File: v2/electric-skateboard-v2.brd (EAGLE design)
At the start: 88.9 x 55.9 mm, 60 parts, among them J1 ZX62D-B-5P8, U1 SPX29300, U2 LDO, U3 MPU-9150, U5 STM32F4V

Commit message: In theory I could ship this layout but I'm ashamed of it. It's gross.
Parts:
- removed TP3, TP4: TPTP06R, testpad:TP06R
- CTS1: value 25MHz -> (none); device crystal:CTS406 -> adafruit:CTS406
- JP6: value (none) -> PRESSA
- JP7: value (none) -> PRESSB
- JP9: value (none) -> LCD
- moved JP9 153.5 mm to (28.7, 51.6), turned to 180 degrees
- moved JP8 130.1 mm to (54.9, 21.8), turned to 180 degrees
- moved C9 122.6 mm to (40.4, 22.9), turned to 90 degrees
- moved R17 121.8 mm to (47.2, 22.1), turned to 270 degrees
- moved R15 116.3 mm to (47.2, 19.1), turned to 90 degrees
- moved JTAG1 104.4 mm to (36.1, 21.1), turned to 0 degrees
- moved JP7 100.6 mm to (11.7, 23.6)
- moved R14 91.3 mm to (22.6, 21.8), turned to 270 degrees
- moved JP6 89.9 mm to (11.7, 18.5)
- moved JP4 88.1 mm to (34.3, 53.1)
- moved C15 87.4 mm to (33.5, 44.7), turned to 0 degrees
- moved J1 87.4 mm to (2.03, 5.08), turned to 270 degrees
- moved C18 86.1 mm to (33.5, 45.8), turned to 0 degrees
- moved Q2 82.9 mm to (46.5, 48.3)
- moved R12 81.4 mm to (7.62, 18.5), turned to 90 degrees
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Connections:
- net N$1 renamed SDA2
- net N$10 renamed ESCB
- net N$12 renamed ESCA
- net N$7 renamed SCL2
- net CLKOUT: now also U5.PE1; no longer U5.PD9
- net GND: no longer TP3.TP, TP4.TP
- net INT: now also U5.PE0; no longer U5.PD8
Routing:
- net 5V: track 2.61 -> 109.5 mm, vias 0 -> 2
- net ANALOG_IN_PC3: track 0.00 -> 67.7 mm, vias 0 -> 2
- net HALLA_DIGINPUT: track 0.00 -> 59.8 mm, vias 0 -> 2
- net FS_VBUS: track 0.00 -> 58.8 mm, vias 0 -> 2
- net FS_ID: track 0.00 -> 58.5 mm, vias 0 -> 2
- net 3.3V: track 13.8 -> 72.1 mm, vias 0 -> 11
- net FS_DP: track 0.00 -> 56.6 mm, vias 0 -> 2
- net HALLB_DIGINPUT: track 0.00 -> 55.3 mm, vias 0 -> 2
- net FS_DM: track 0.00 -> 54.3 mm, vias 0 -> 2
- net ANALOG_IN_PC2: track 0.00 -> 50.8 mm, vias 0 -> 2
- net SCL1: track 0.00 -> 33.8 mm
- net CLKOUT: track 0.00 -> 33.7 mm, vias 0 -> 2
- net VIN: track 0.00 -> 30.7 mm
- net INT: track 0.00 -> 27.9 mm, vias 0 -> 2
- net SDA1: track 0.00 -> 27.2 mm, vias 0 -> 2
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- added copper zone on layer 1, net 3.3V
- added copper zone on layer 16, net 5V
- added copper zone on layer 1, net GND
- added copper zone on layer 16, net GND
- added copper zone on layer 1, net OSC_IN1
- added copper zone on layer 1, net OSC_OUT1
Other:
- board size 88.9 x 55.9 mm -> 59.4 x 55.9 mm

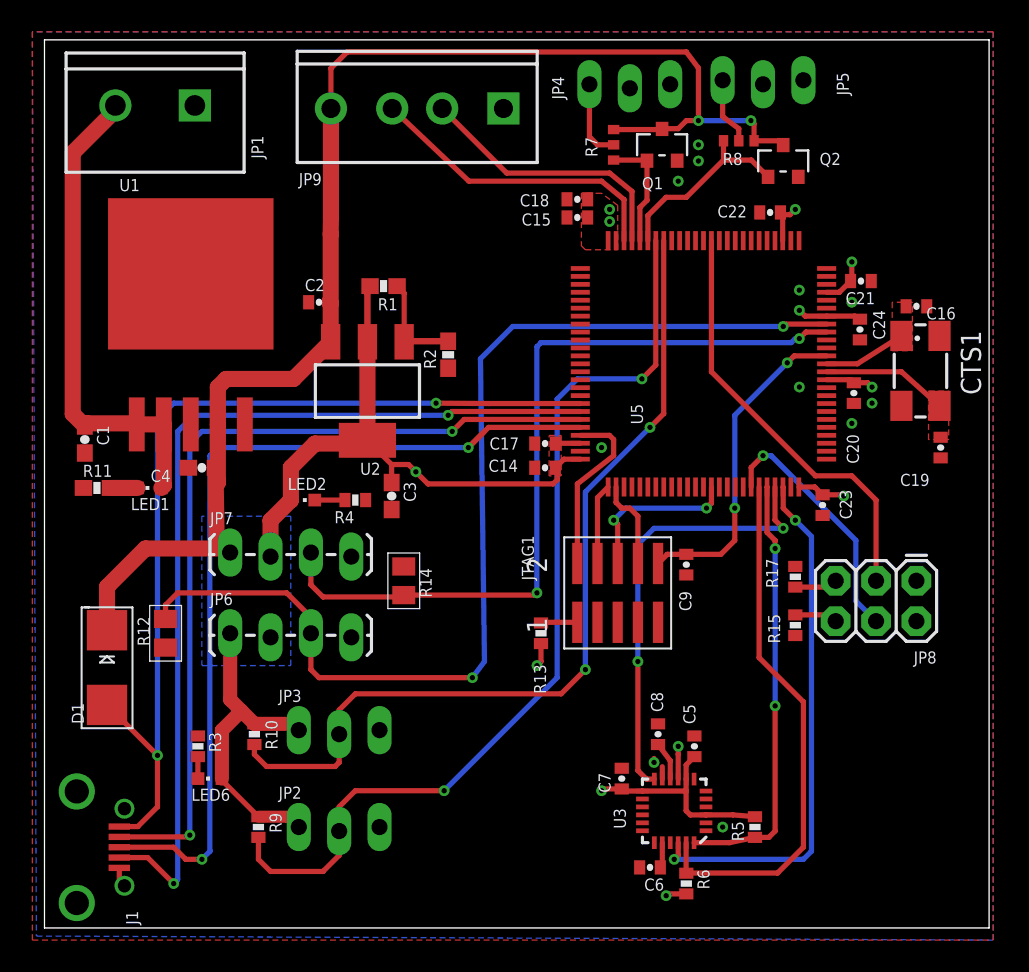
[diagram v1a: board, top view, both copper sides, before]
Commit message: Needs final review but otherwise layout is done.
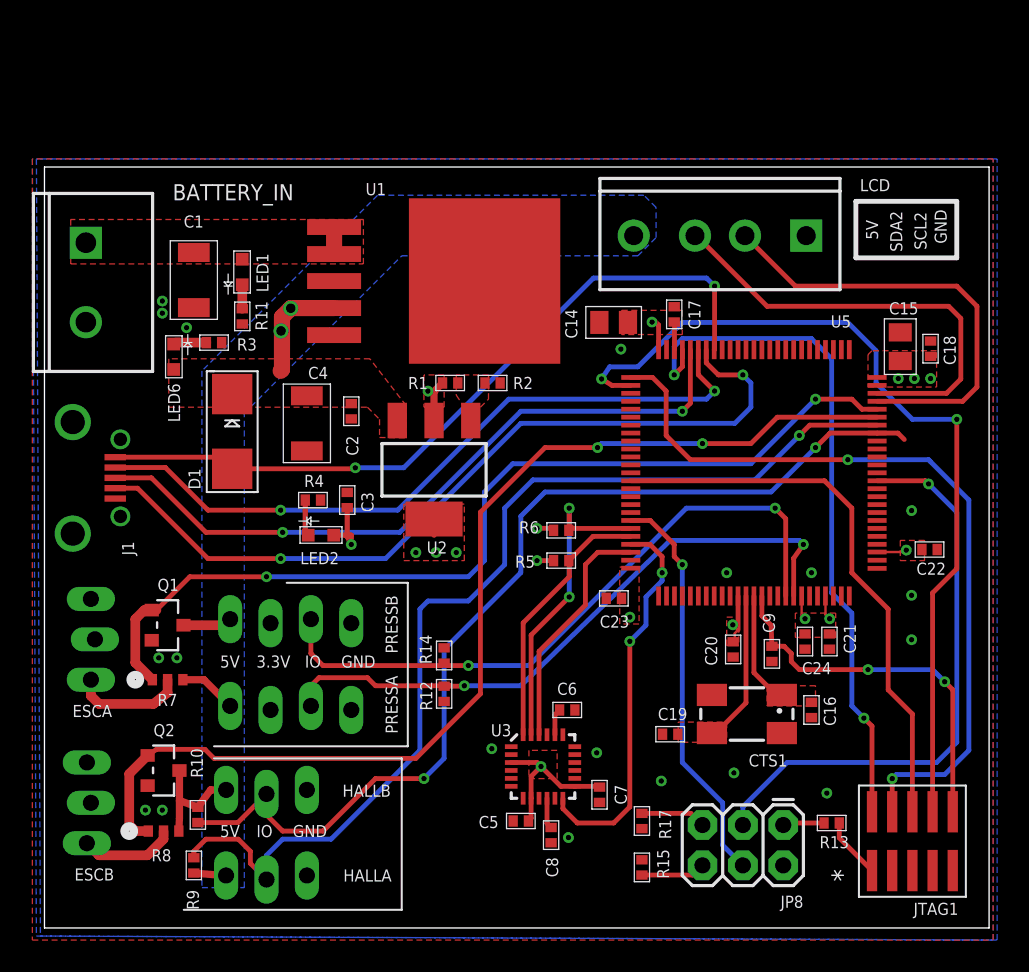
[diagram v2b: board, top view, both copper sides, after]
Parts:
- removed JP1: BATT, SparkFun-Connectors:SCREWTERMINAL-5MM-2
- removed JP2: HALLA, SparkFun-Connectors:1X03_LOCK_LONGPADS
- removed JP3: HALLB, SparkFun-Connectors:1X03_LOCK_LONGPADS
- removed JP4: ESCA, SparkFun-Connectors:1X03_LOCK_LONGPADS
- removed JP5: ESCB, SparkFun-Connectors:1X03_LOCK_LONGPADS
- removed JP6: PRESSA, SparkFun-Connectors:1X04_LOCK_LONGPADS
- removed JP7: PRESSB, SparkFun-Connectors:1X04_LOCK_LONGPADS
- removed JP9: LCD, SparkFun-Connectors:SCREWTERMINAL-3.5MM-4_LOCK
- added BATTERY_IN: BATT, SparkFun-Connectors:SCREWTERMINAL-5MM-2
- added ESCA, ESCB, HALLA, HALLB: (no value), SparkFun-Connectors:1X03_LOCK_LONGPADS
- added LCD: (no value), SparkFun-Connectors:SCREWTERMINAL-3.5MM-4_LOCK
- added PRESSA, PRESSB: (no value), SparkFun-Connectors:1X04_LOCK_LONGPADS
- C1, C4: device SparkFun-Passives:0603-CAP -> max-viz:RLC-1210
- C14, C15: device SparkFun-Passives:0402-CAP -> max-viz:RLC-0805
- C16, C17, C18, C19, C2, C20, C21, C22, C23, C24, C5, C6, C7, C8, C9: device SparkFun-Passives:0402-CAP -> max-viz:RLC-0402
- C3: device SparkFun-Passives:0603-CAP -> max-viz:RLC-0402
- LED1, LED2, LED6: device led:CHIPLED_0603 -> max-viz:LED0603
- R1, R11, R2: device SparkFun-Passives:0603-RES -> max-viz:RLC-0402
- R10, R13, R15, R17, R3, R4, R5, R6, R9: device SparkFun-Passives:0402-RES -> max-viz:RLC-0402
- R12, R14: device max-viz:RLC-0805 -> max-viz:RLC-0402
- moved R8 56.5 mm to (7.49, 6.10)
- moved Q2 54.7 mm to (7.49, 9.91), turned to 270 degrees
- moved R7 43.8 mm to (7.75, 15.6), turned to 0 degrees
- moved Q1 43.4 mm to (7.75, 19.1), turned to 270 degrees
- moved LED6 26.6 mm to (8.13, 35.9), turned to 180 degrees
- moved C16 26.2 mm to (48.3, 13.7), turned to 90 degrees
- moved R3 25.4 mm to (10.7, 36.8), turned to 180 degrees
- moved C19 24.8 mm to (39.4, 12.2), turned to 0 degrees
- moved JTAG1 24.2 mm to (54.6, 5.46)
- moved CTS1 24.2 mm to (44.2, 13.5), turned to 180 degrees
- moved C18 24.1 mm to (55.8, 36.4), turned to 270 degrees
- moved R6 23.6 mm to (32.5, 25.0), turned to 180 degrees
- moved C22 23.5 mm to (55.7, 23.8), turned to 180 degrees
- moved J1 23.2 mm to (1.78, 28.3)
- moved C21 22.8 mm to (49.4, 18.0), turned to 90 degrees
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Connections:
- net 3.3V: now also PRESSA.2, PRESSB.2; no longer JP6.2, JP7.2
- net 5V: now also HALLA.1, HALLB.1, LCD.4, PRESSA.1, PRESSB.1; no longer JP2.1, JP3.1, JP6.1, JP7.1, JP9.4
- net ANALOG_IN_PC2: now also PRESSB.3; no longer JP7.3
- net ANALOG_IN_PC3: now also PRESSA.3; no longer JP6.3
- net ESCA: now also ESCA.1; no longer JP4.1
- net ESCB: now also ESCB.1; no longer JP5.1
- net GND: now also BATTERY_IN.2, HALLA.3, HALLB.3, LCD.1, PRESSA.4, PRESSB.4; no longer JP1.1, JP2.3, JP3.3, JP6.4, JP7.4, JP9.1
- net HALLA_DIGINPUT: now also HALLA.2; no longer JP2.2
- net HALLB_DIGINPUT: now also HALLB.2; no longer JP3.2
- net SCL2: now also LCD.2; no longer JP9.2
- net SDA2: now also LCD.3; no longer JP9.3
- net VIN: now also BATTERY_IN.1; no longer JP1.2
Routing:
- net 5V: track 109.5 -> 23.2 mm
- net ESCB_PWM_OUT: track 12.2 -> 68.1 mm, vias 0 -> 2
- net ESCA_PWM_OUT: track 7.33 -> 59.5 mm, vias 0 -> 2
- net TDI: track 5.68 -> 54.9 mm, vias 0 -> 2
- net TCK: track 5.09 -> 49.5 mm, vias 0 -> 2
- net 3.3V: track 72.1 -> 34.0 mm, vias 11 -> 17
- net TMS: track 11.1 -> 43.8 mm, vias 0 -> 2
- net VIN: track 30.7 -> 1.70 mm
- net ANALOG_IN_PC3: track 67.7 -> 40.7 mm
- net TDO: track 10.4 -> 35.3 mm, vias 2 -> 0
- net CLKOUT: track 33.7 -> 15.1 mm, vias 2 -> 0
- net SCL1: track 33.8 -> 20.7 mm, vias 0 -> 2
- net FS_DP: track 56.6 -> 44.3 mm
- net FS_VBUS: track 58.8 -> 47.2 mm
- net SCL2: track 17.1 -> 28.2 mm
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- added copper zone on layer 15, net 3.3V
- added copper zone on layer 1, net 5V
- added copper zone on layer 2, net GND
- added copper zone on layer 1, net N$21
- added copper zone on layer 1, net VIN
- removed copper zone on layer 2, net 3.3V
- removed copper zone on layer 15, net GND
- removed copper zone on layer 2, net VIN
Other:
- board size 59.4 x 55.9 mm -> 59.4 x 47.9 mm
- board text added: "3.3V"
- board text added: "5V"
- board text added: "GND"
- board text added: "IO"
- board text added: "SCL2"
- board text added: "SDA2"

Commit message: Shipping it.
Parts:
- removed R1: 240, max-viz:RLC-0402
- removed R2: 390, max-viz:RLC-0402
- removed U2: LDO, SparkFun-PowerIC:SOT223
- added U4: AAT3221IGV-3.3-T1, SparkFun-DigitalIC:SOT23-5
- C3: device max-viz:RLC-0402 -> max-viz:RLC-1210
- C5, C8: value 0.1uF -> 100nF
- C6: value 2.2nF -> 100nF
- moved R4 17.7 mm to (33.6, 33.0), turned to 90 degrees
- moved LED2 16.5 mm to (31.4, 33.5), turned to 90 degrees
- moved C3 10.0 mm to (27.9, 31.6), turned to 270 degrees
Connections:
- removed net N$21: R1.1, R2.2, U2.1
- net 3.3V: now also U4.5; no longer R1.2, U2.2, U2.4
- net 5V: now also U4.1, U4.3; no longer U2.3
- net GND: now also CTS1.2, CTS1.4, U4.2; no longer R2.1
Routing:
- net GND: track 0.00 -> 7.74 mm, vias 19 -> 41
- net 3.3V: track 34.0 -> 32.3 mm, vias 17 -> 13
- net N$2: track 2.40 -> 1.41 mm
- removed copper zone on layer 1, net N$21
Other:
- board text added: "*"
- board text added: "ESkate Board v2 jeh.wicker@gmail.com May 18 2015"

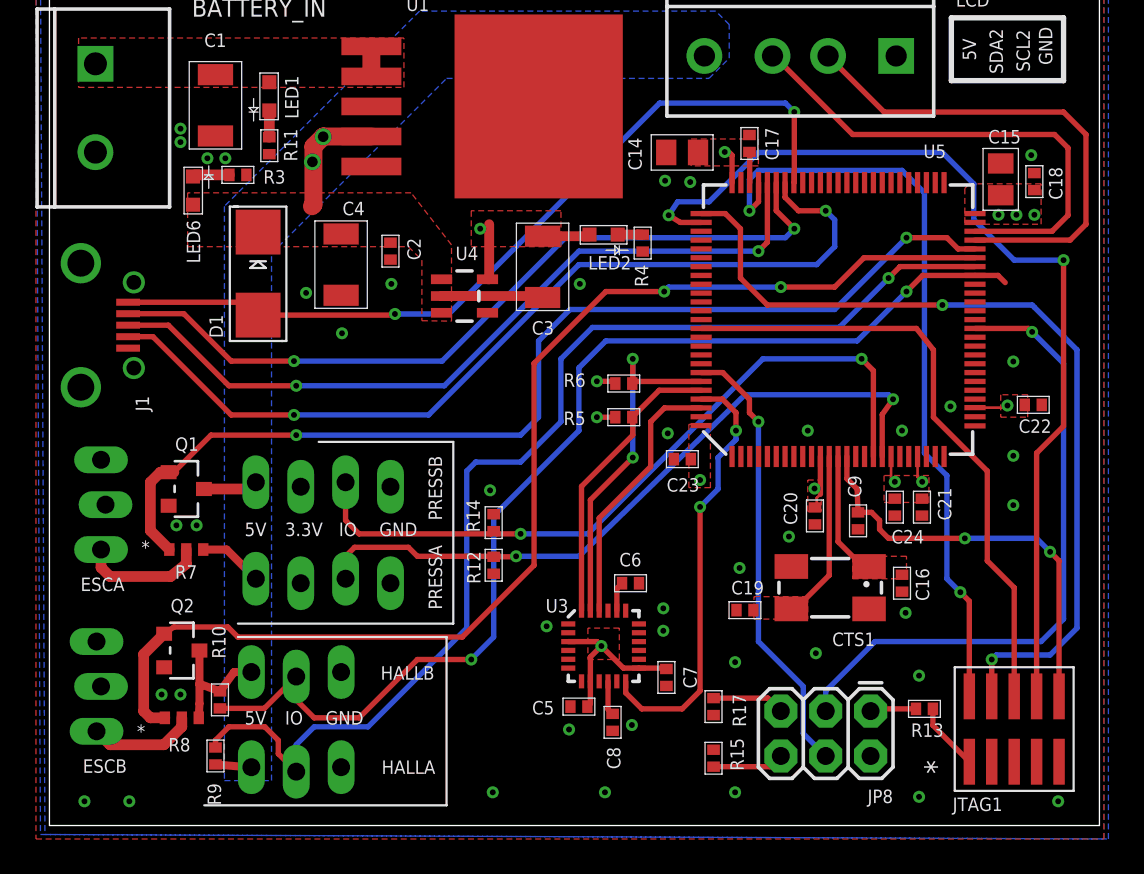
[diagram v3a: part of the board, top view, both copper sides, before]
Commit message: Added button. Changed LDO.
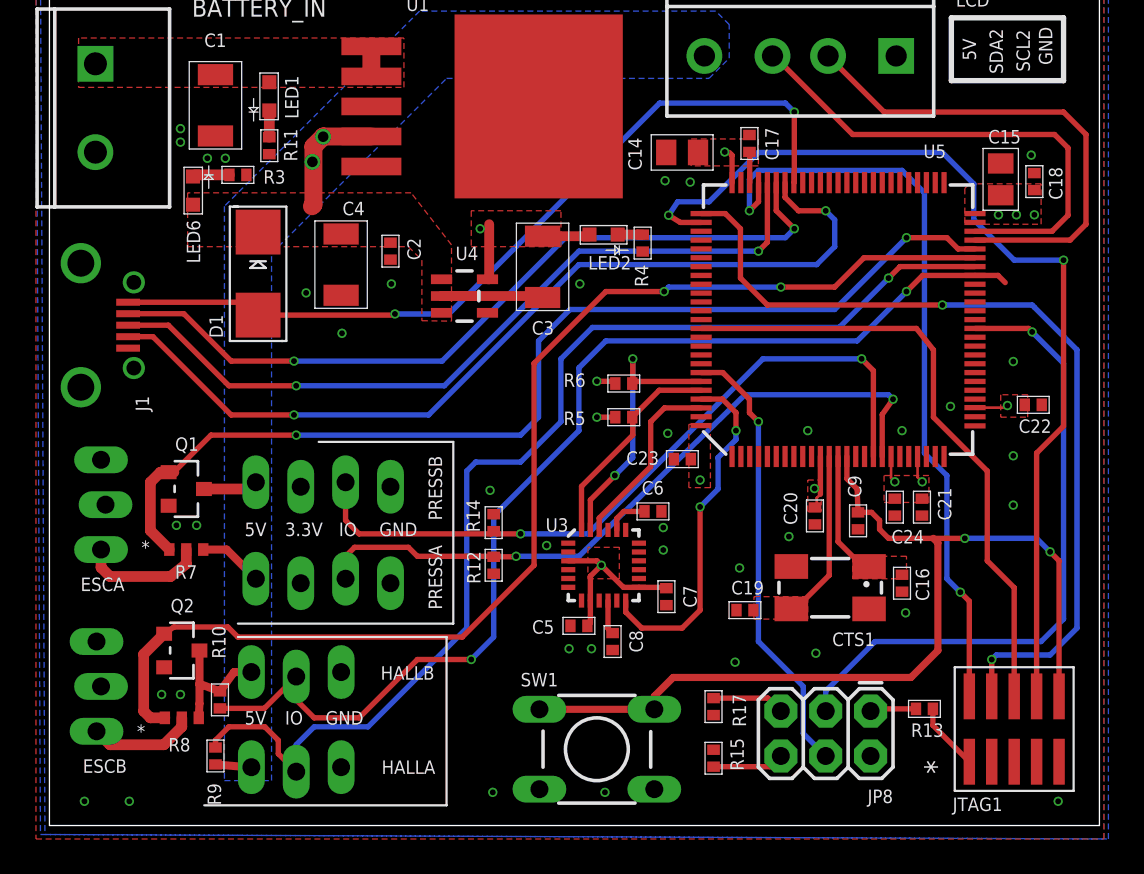
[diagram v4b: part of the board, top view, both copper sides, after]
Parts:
- added SW1: (no value), GeekAmmo:TAC-SWITCH-PTH
- moved C5 4.57 mm to (30.0, 11.3)
- moved C7 4.57 mm to (34.9, 13.0)
- moved C8 4.57 mm to (31.9, 10.4)
- moved U3 4.57 mm to (31.4, 14.7)
- moved C6 4.26 mm to (34.2, 17.8)
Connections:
- net GND: now also SW1.3, SW1.4
- net NRST: now also SW1.1, SW1.2
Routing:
- net NRST: track 23.9 -> 54.7 mm
- net SDA1: track 16.7 -> 12.1 mm
- net SCL1: track 20.7 -> 16.1 mm
- net CLKOUT: track 15.1 -> 10.5 mm
- net INT: track 24.5 -> 20.0 mm
- net N$4: track 1.68 -> 2.38 mm
- net GND: vias 41 -> 38
